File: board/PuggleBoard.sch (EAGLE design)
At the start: 131 parts, among them U1 LMP7704, U10 SN65LVDS2, U11 SN65LVDS1, U12 SN65LVDS1, U13 SN65LVDS1, U14 SN65MLVD201D, U15 24C, U2 ADS8331, U3 OPA4209, U4 AD5686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

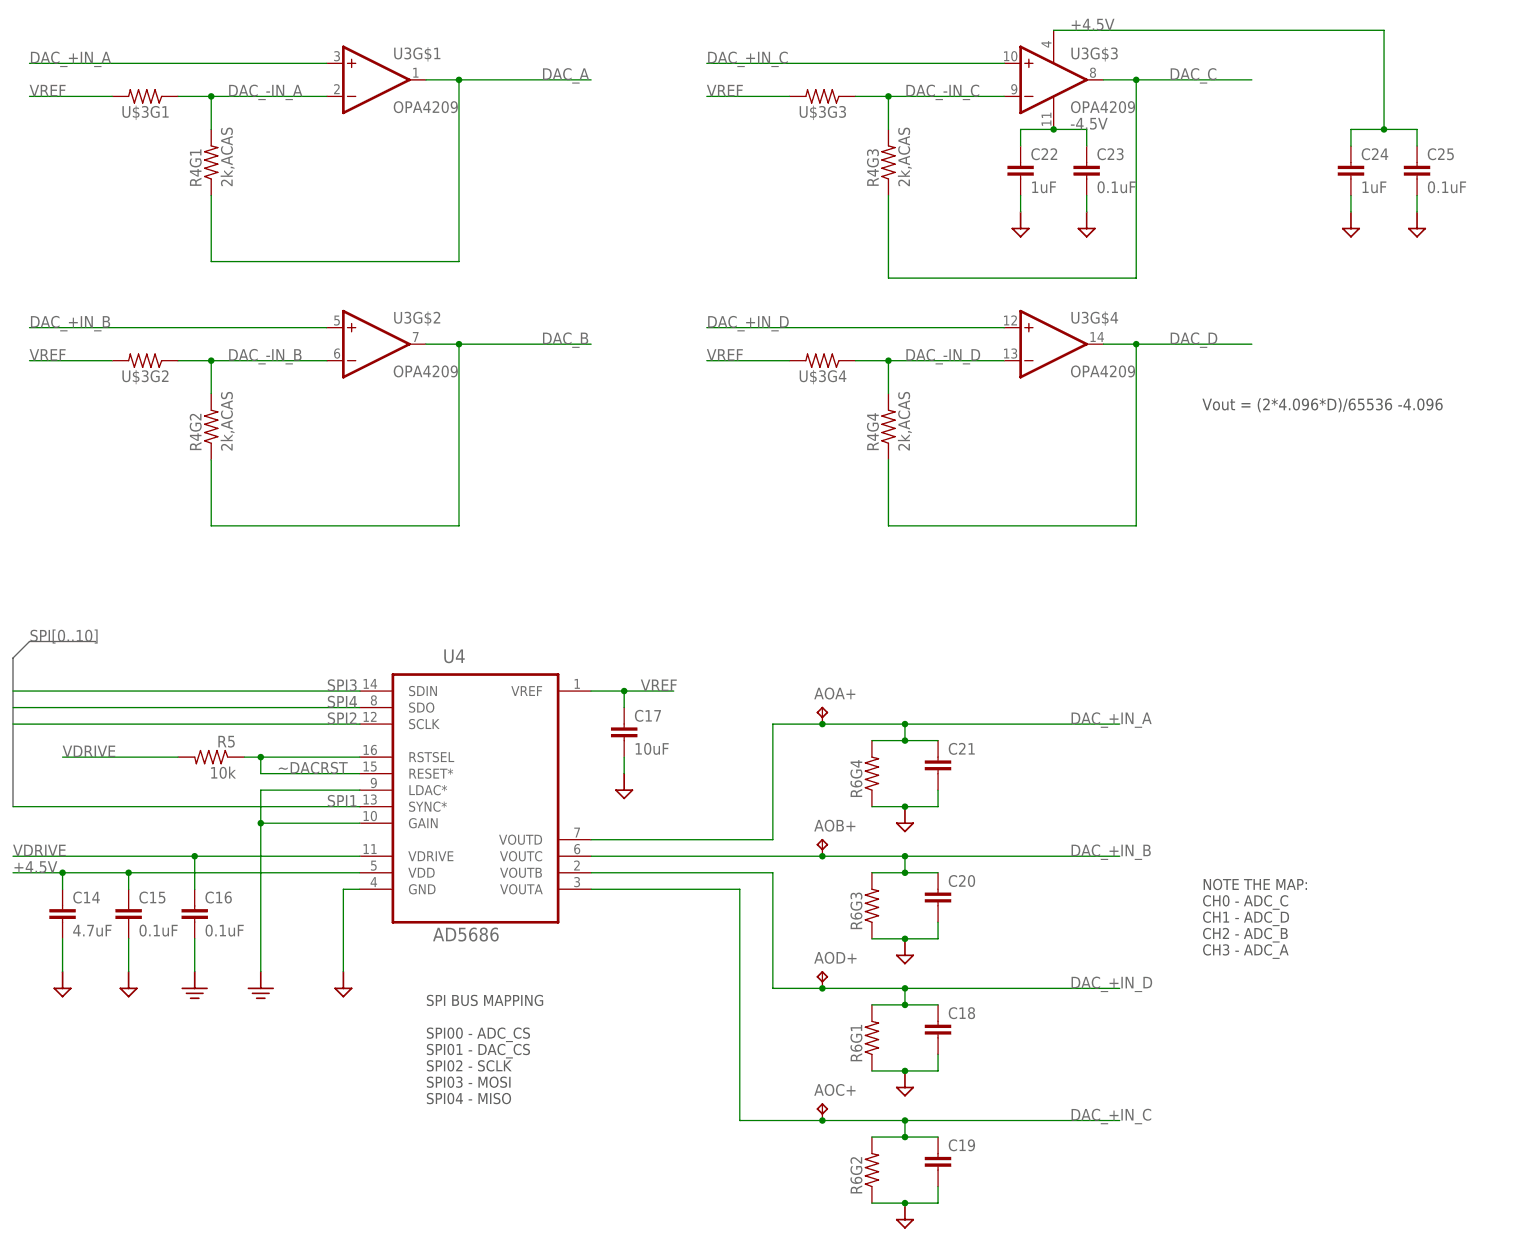
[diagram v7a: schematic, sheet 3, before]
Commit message: Board is ready for Edgar to look at. There is one strange DRC error, but that can be resolved later. Also, silk screens are a mess, but Edgar can see the layout at least.
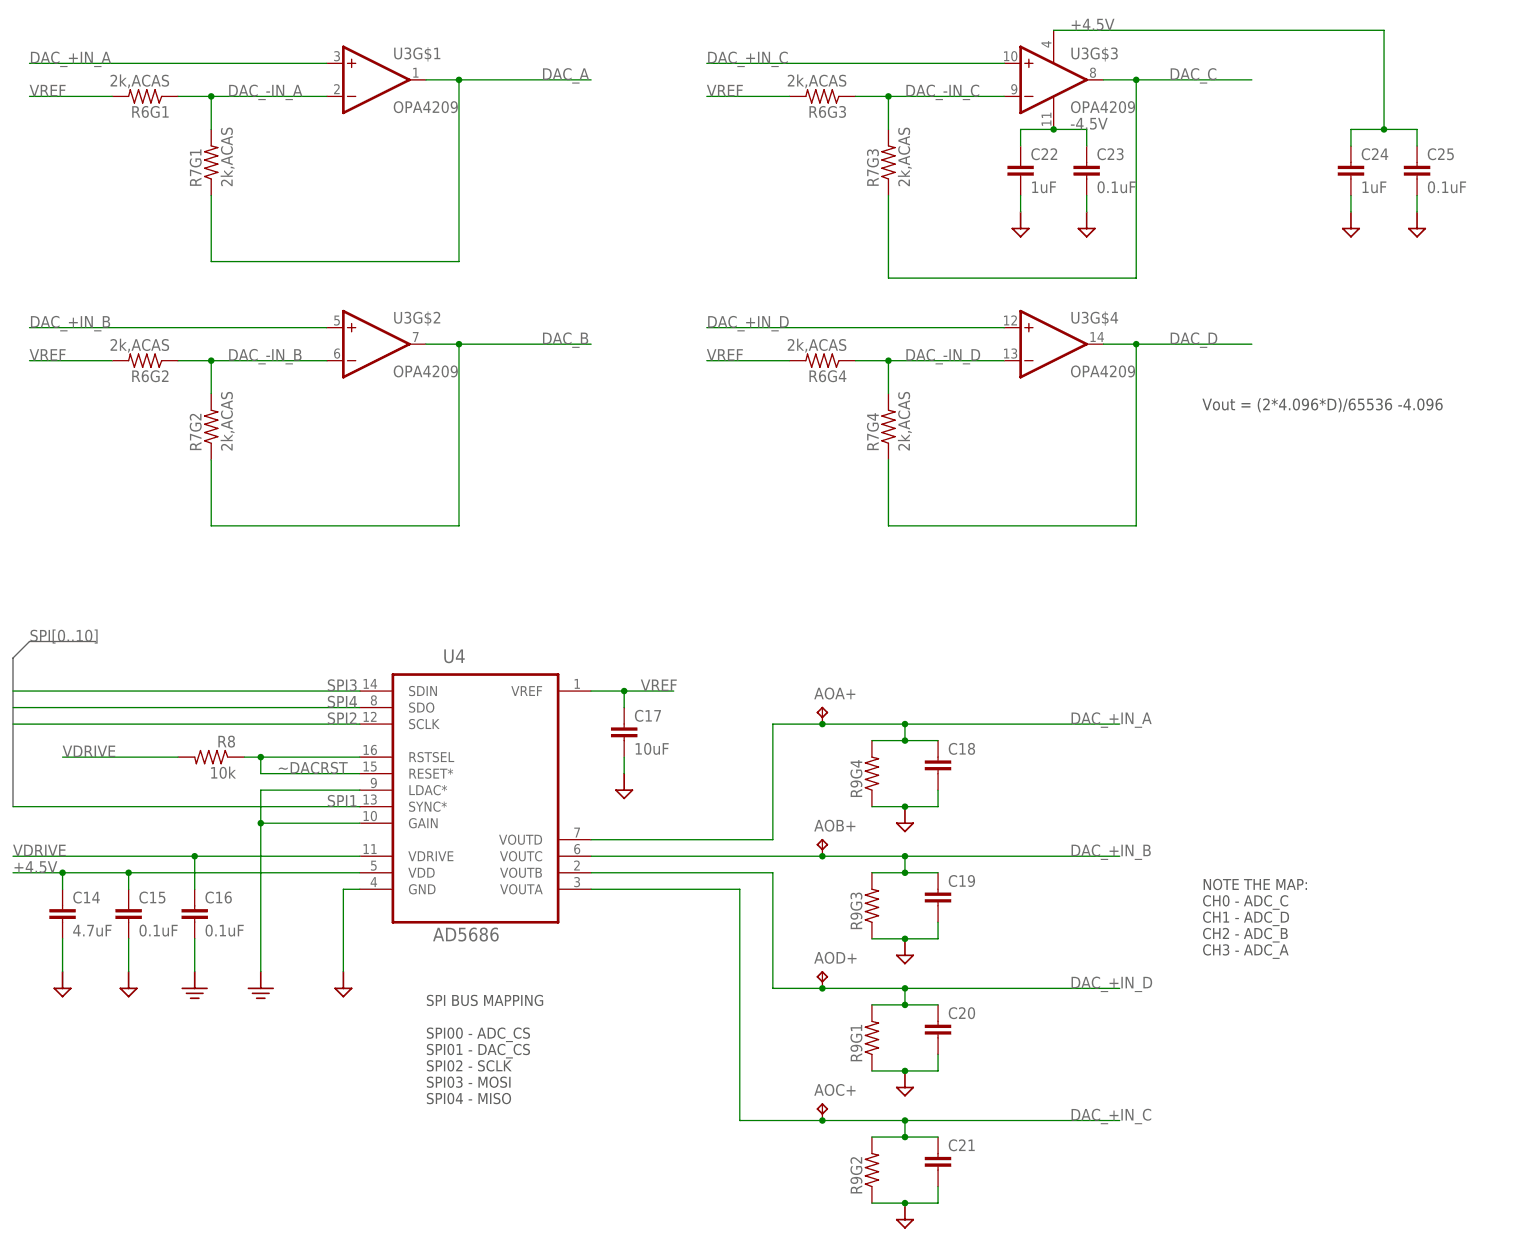
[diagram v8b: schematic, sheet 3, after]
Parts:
- removed $2_103_$: 2k,ACAS, puggleboard:RX4_0612
- removed $2_104_$: 1k,ACAS, puggleboard:RX4_0612
- removed U$3: (no value), puggleboard:RX4_0612
- added R27: 10k, puggleboard:R_0603
- added R28, R29: 5.6k, puggleboard:R_0603
- C36: value 10uF -> 22uF
- C38: value 22uF -> 10uF
- C40: value 1uF -> 47uF; device puggleboard:C_0603 -> puggleboard:C-POL_0807
- C42: value 0.1uF -> 1uF
- C45: value 4.7uF -> 0.1uF; device puggleboard:C_1206 -> puggleboard:C_0603
- C46: value 0.1uF -> 4.7uF; device puggleboard:C_0603 -> puggleboard:C_1206
- C51, C56: value 1nF -> 0.1uF
- C55, C57: value 0.1uF -> 1nF
- C58: value 47uF -> 0.1uF; device puggleboard:C-POL_0807 -> puggleboard:C_0603
- R1: value 1k -> 2k,ACAS; device puggleboard:RX4_0603 -> puggleboard:RX4_0612
- R10: value 13.7k -> 130k
- R11: value 4.7k -> 13.7k
- R12: value 60.4k -> 4.7k
- R13: value 1k -> 13.7k
- R14, R24: value 10k -> 4.7k
- R15: value 6k -> 60.4k
- R16: value 2k -> 1k; device puggleboard:TRIM_US-SM-42/43W -> puggleboard:R_0603
- R17: value 2k -> 10k
- R18: value 10k -> 6k
- R19: value 100 -> 2k; device puggleboard:R_0603 -> puggleboard:TRIM_US-SM-42/43W
- R2: value 10 -> 1k,ACAS; device puggleboard:R_0603 -> puggleboard:RX4_0612
- R20: value 150 -> 2k
- R21: value 4.7k -> 10k
- R22: value 4.7k -> 100
- R23: value 4.7k -> 150
- R25, R26: value 5.6k -> 4.7k
- R3: value 10k -> 1k; device puggleboard:R_0603 -> puggleboard:RX4_0603
- R4: value 2k,ACAS -> 10; device puggleboard:RX4_0612 -> puggleboard:R_0603
- R6: value (none) -> 2k,ACAS; device puggleboard:RX4_0603 -> puggleboard:RX4_0612
- R7: value 130k -> 2k,ACAS; device puggleboard:R_0603 -> puggleboard:RX4_0612
- R8: value 13.7k -> 10k
- R9: value 4.7k -> (none); device puggleboard:R_0603 -> puggleboard:RX4_0603
- U14: value SN65MLVD201D -> SN65MLVD201
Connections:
- net +4.5V: now also C38.1, C41.2, C45.1; no longer C37.1, C40.2, C44.1
- net +4.5V_PRE: now also R13.1; no longer R10.1
- net -4.5V: now also C37.1; no longer C36.1
- net -4.5V_PRE: now also R11.1; no longer R8.1
- net ADC_-IN_A: now also R1G1.1, R2G1.2; no longer $2_103_$G1.1, $2_104_$G1.2
- net ADC_-IN_B: now also R1G2.1, R2G2.2; no longer $2_103_$G2.1, $2_104_$G2.2
- net ADC_-IN_C: now also R1G3.1, R2G3.2; no longer $2_103_$G3.1, $2_104_$G3.2
- net ADC_-IN_D: now also R1G4.1, R2G4.2; no longer $2_103_$G4.1, $2_104_$G4.2
- net ADC_A: now also R1G1.2; no longer $2_103_$G1.2
- net ADC_A+: now also R2G1.1, R3G1.2; no longer $2_104_$G1.1, R1G1.2
- net ADC_B: now also R1G2.2; no longer $2_103_$G2.2
- net ADC_B+: now also R2G2.1, R3G2.2; no longer $2_104_$G2.1, R1G2.2
- net ADC_C: now also R1G3.2; no longer $2_103_$G3.2
- net ADC_C+: now also R2G3.1, R3G3.2; no longer $2_104_$G3.1, R1G3.2
- net ADC_D: now also R1G4.2; no longer $2_103_$G4.2
- net ADC_D+: now also R2G4.1, R3G4.2; no longer $2_104_$G4.1, R1G4.2
- net AGND1: now also R13.2, R14.1; no longer R10.2, R11.1
- net AGND2: now also R11.2, R12.1; no longer R8.2, R9.1
- net DAC_+IN_A: now also C18.1, R9G4.2; no longer C21.1, R6G4.2
- net DAC_+IN_B: now also C19.1, R9G3.2; no longer C20.1, R6G3.2
- net DAC_+IN_C: now also C21.1, R9G2.2; no longer C19.1, R6G2.2
- net DAC_+IN_D: now also C20.1, R9G1.2; no longer C18.1, R6G1.2
- net DAC_-IN_A: now also R6G1.1, R7G1.2; no longer R4G1.2, U$3G1.1
- net DAC_-IN_B: now also R6G2.1, R7G2.2; no longer R4G2.2, U$3G2.1
- net DAC_-IN_C: now also R6G3.1, R7G3.2; no longer R4G3.2, U$3G3.1
- net DAC_-IN_D: now also R6G4.1, R7G4.2; no longer R4G4.2, U$3G4.1
- net DAC_A: now also R7G1.1; no longer R4G1.1
- net DAC_B: now also R7G2.1; no longer R4G2.1
- net DAC_C: now also R7G3.1; no longer R4G3.1
- net DAC_D: now also R7G4.1; no longer R4G4.1
- net GND: now also C40.-, C42.1, C58.2, R10.2, R12.2, R14.2, R20.2, R9G1.1, R9G2.1, R9G3.1, R9G4.1; no longer C40.1, C42.2, C58.-, R11.2, R17.2, R6G1.1, R6G2.1, R6G3.1, R6G4.1, R7.2, R9.2
- net I2C2_SCL: now also R28.1; no longer R25.1
- net I2C2_SDA: now also R29.1; no longer R26.1
- net MISO1_N: now also R22.2; no longer R19.2
- net MISO1_P: now also R22.1; no longer R19.1
- net N$10: now also R18.2, R19.E; no longer R15.2, R16.E
- net N$14: now also R24.1; no longer R21.1
- net N$16: now also R4.1; no longer R2.1
- net N$18: now also R25.1; no longer R22.1
- net N$19: now also R26.1; no longer R23.1
- net N$20: now also R16.1; no longer R13.1
- net N$22: now also R27.1; no longer R24.1
- net N$28: now also C43.1, R17.1; no longer C42.1, R14.1
- net N$32: now also C42.2; no longer C41.2
- net N$37: now also R10.1; no longer R7.1
- net N$4: now also C44.1, R19.S; no longer C43.1, R16.S
- net N$40: now also R3G1.1; no longer R1G1.1
- net N$41: now also R3G2.1; no longer R1G2.1
- net N$42: now also R3G3.1; no longer R1G3.1
- net N$43: now also R3G4.1; no longer R1G4.1
- net N$45: now also R15.2; no longer R12.2
- net N$8: now also R19.A, R20.1; no longer R16.A, R17.1
- net N$9: now also R21.2; no longer R18.2
- net SYNC_N: now also R23.2; no longer R20.2
- net SYNC_P: now also R23.1; no longer R20.1
- net VBIAS: now also C47.1, R21.1; no longer C46.1, R18.1
- net VDD_5V: now also C39.+, L2.1, R16.2; no longer C58.+, L1.1, R13.2
- net VDD_POST_LC: now also L2.2; no longer L1.2
- net VDRIVE: now also C40.+, C58.1, R27.2, R28.2, R29.2, R8.2; no longer C39.+, C47.1, R21.2, R22.2, R23.2, R3.2
- net VOUT-: now also C36.1, L1.1, R15.1; no longer C38.1, L2.1, R12.1
- net VREF: now also R18.1, R4.2, R6G1.2, R6G2.2, R6G3.2, R6G4.2; no longer R15.1, R2.2, U$3G1.2, U$3G2.2, U$3G3.2, U$3G4.2
- net VREF_PRE: now also C46.1, R17.2; no longer C45.1, R14.2
- net VSS_POST_LC: now also L1.2; no longer L2.2
- net ~ADCRST: now also R5.1; no longer R3.1
- net ~DACRST: now also R8.1; no longer R5.1
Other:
- moved on the sheet: C18, C19, C20, C21, C36, C37, C38, C39, C41, C42, C43, C44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
